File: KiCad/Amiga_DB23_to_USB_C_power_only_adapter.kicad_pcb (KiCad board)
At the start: 2 copper layers, 33.5 x 34 mm, 4 parts, among them J1 DB23_Male, J2 UJC-HP-3-SMT-TR

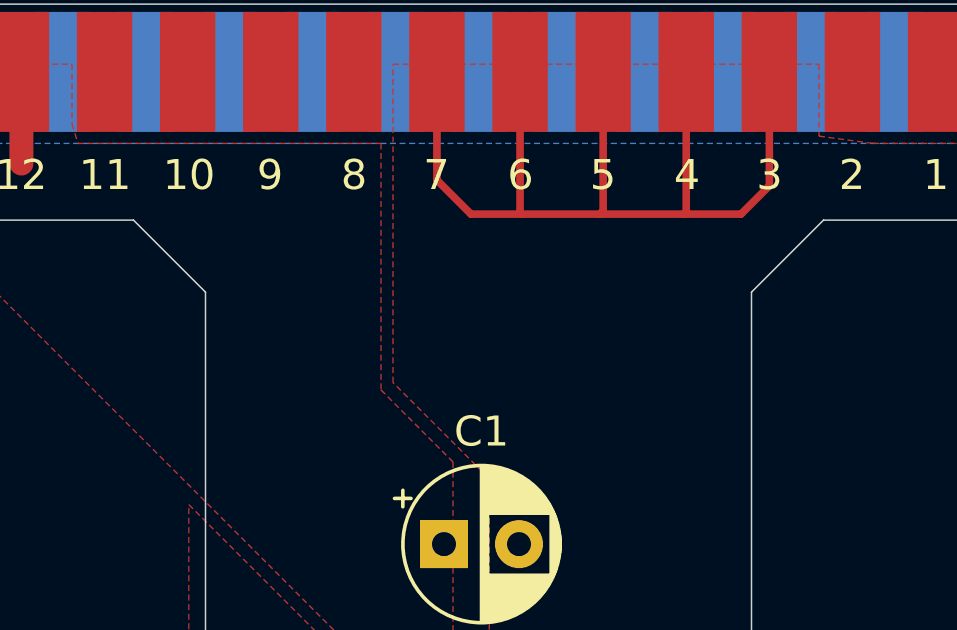
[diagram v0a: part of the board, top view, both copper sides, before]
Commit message: Added silkscreen text and OSHW-logo
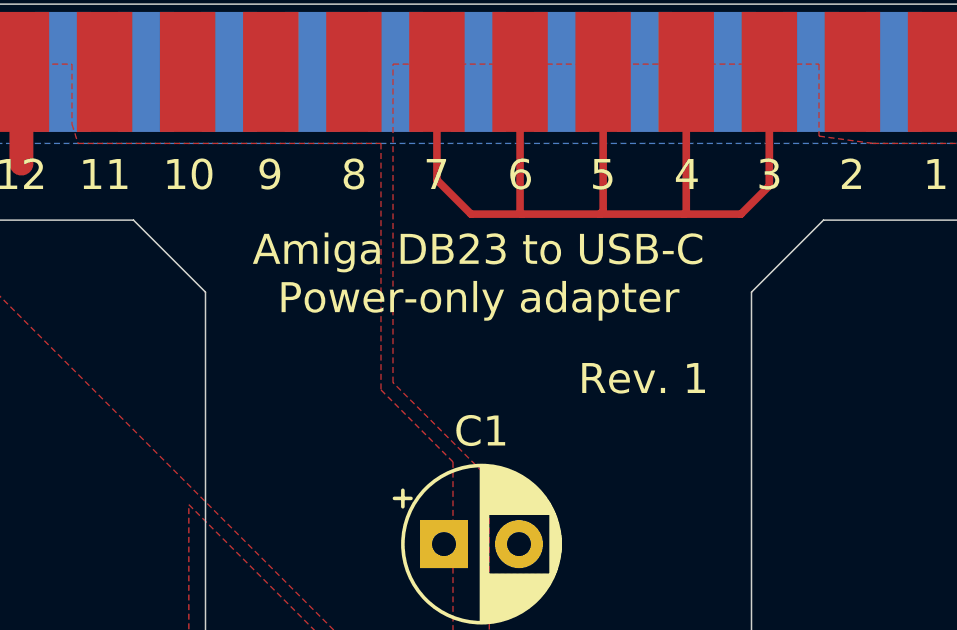
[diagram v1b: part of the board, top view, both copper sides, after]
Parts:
- added REF**: OSHW-Logo2_14.6x12mm_SilkScreen, Symbol:OSHW-Logo2_14.6x12mm_SilkScreen, B.Cu at (106.5, 63.8)
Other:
- board text added: "(C) 2023 Design by J.Bilander"
- board text added: "Amiga DB23 to USB-C Power-only adapter"
- board text added: "Rev. 1"
